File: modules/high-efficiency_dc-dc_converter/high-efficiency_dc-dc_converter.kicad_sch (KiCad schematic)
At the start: 11 parts

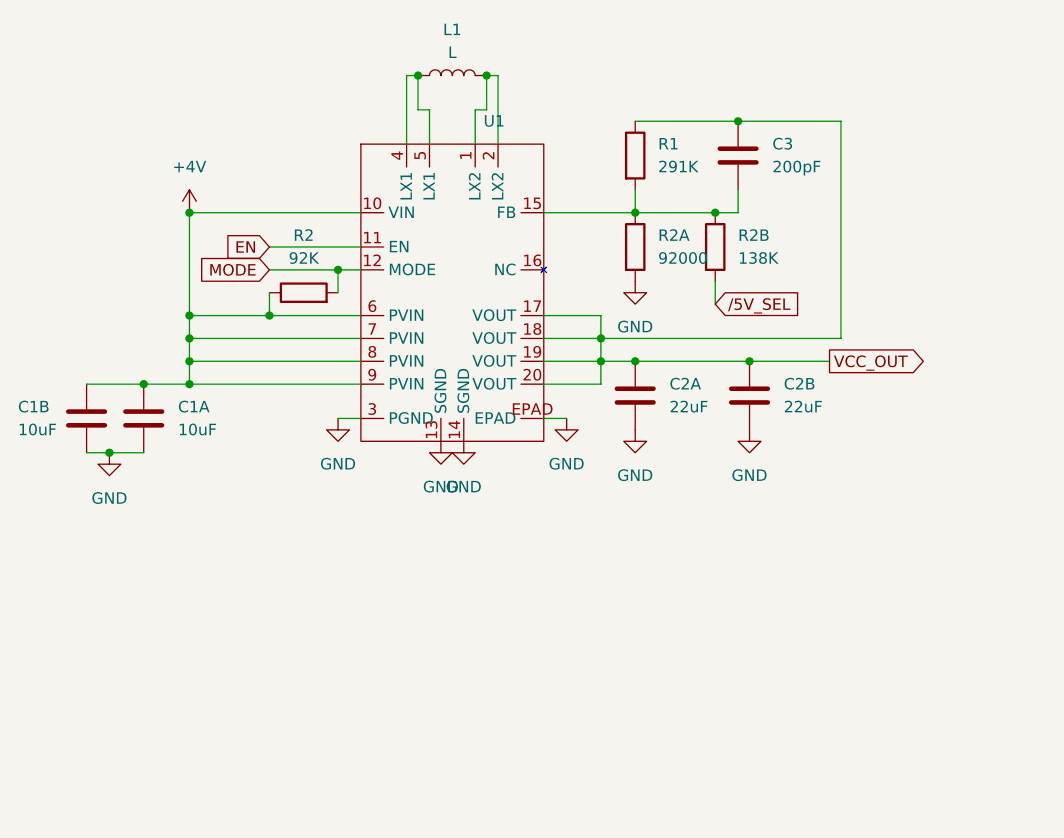
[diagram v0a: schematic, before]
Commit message: assign footprints for passives for DC:DC converter module
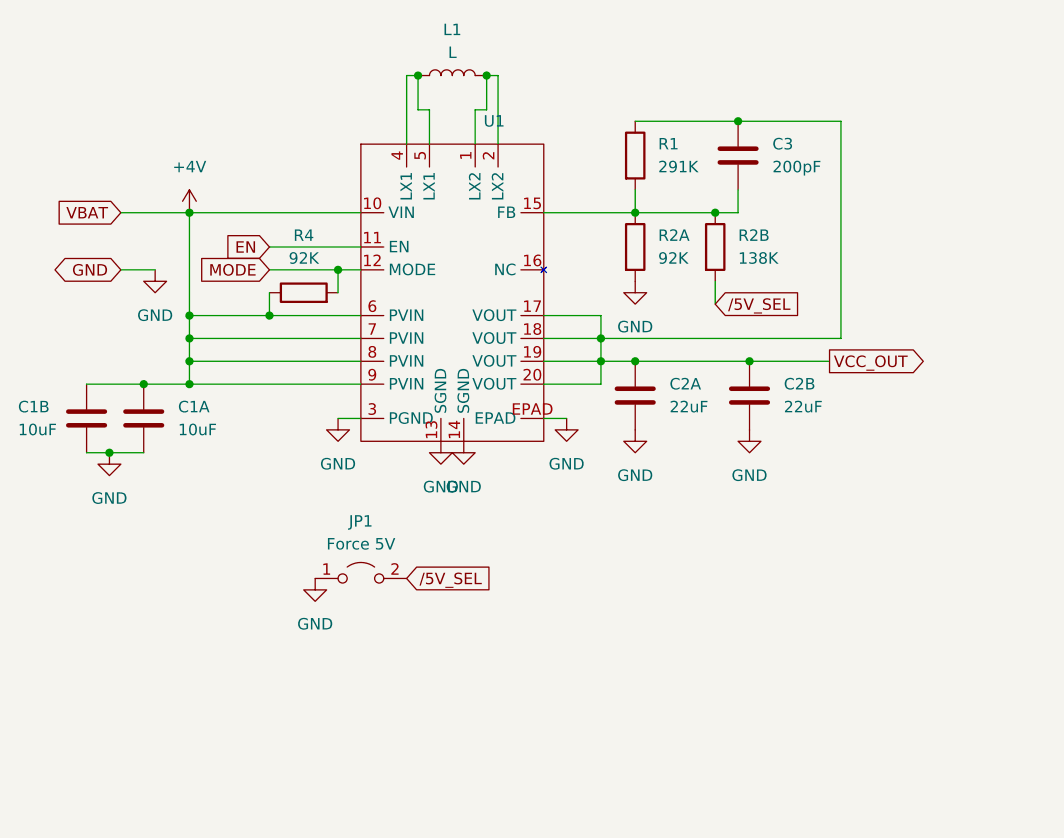
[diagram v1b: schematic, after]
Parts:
- added JP1: Force 5V, Jumper:SolderJumper-2_P1.3mm_Open_RoundedPad1.0x1.5mm, symbol Jumper:Jumper_2_Open
- C1A, C1B, C2A, C2B, C3: footprint (none) -> Capacitor_SMD:C_0805_2012Metric
- L1: footprint (none) -> Inductor_SMD:L_1008_2520Metric
- R1, R2B: footprint (none) -> Resistor_SMD:R_0603_1608Metric
- R2A: value 92000 -> 92K; footprint (none) -> Resistor_SMD:R_0603_1608Metric
- R4: renamed from R2; footprint (none) -> Resistor_SMD:R_0603_1608Metric
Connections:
- net GND: now also JP1.1 (A)
- net /5V_SEL: now also JP1.2 (B)
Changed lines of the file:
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@@
   (junction (at 38.1 77.47) (diameter 0) (color 0 0 0 0)
   )
+  (wire (pts (xy 35.56 58.42) (xy 43.18 58.42))
+    (stroke (width 0) (type default))
+  )
   (wire (pts (xy 82.55 77.47) (xy 88.9 77.47))
     (stroke (width 0) (type default))
@@
     (stroke (width 0) (type default))
   )
+  (wire (pts (xy 35.56 64.77) (xy 39.37 64.77))
+    (stroke (width 0) (type default))
+  )
   (wire (pts (xy 43.18 77.47) (xy 62.23 77.47))
     (stroke (width 0) (type default))
@@
   (wire (pts (xy 68.58 43.18) (xy 67.31 43.18))
     (stroke (width 0) (type default))
+  )
+  (global_label "{slash}5V_SEL" (shape input) (at 67.31 99.06 0) (fields_autoplaced)
+    (effects (font (size 1.27 1.27)) (justify left))
+    (property "Intersheetrefs" "${INTERSHEET_REFS}" (at 78.278 99.06 0)
+      (effects (font (size 1.27 1.27)) (justify left) hide)
+    )
   )
   (global_label "MODE" (shape input) (at 52.07 64.77 180) (fields_autoplaced)
@@
     )
   )
+  (global_label "VBAT" (shape input) (at 35.56 58.42 180) (fields_autoplaced)
+    (effects (font (size 1.27 1.27)) (justify right))
+    (property "Intersheetrefs" "${INTERSHEET_REFS}" (at 28.16 58.42 0)
+      (effects (font (size 1.27 1.27)) (justify right) hide)
+    )
+  )
   (global_label "{slash}5V_SEL" (shape input) (at 101.6 68.58 0) (fields_autoplaced)
     (effects (font (size 1.27 1.27)) (justify left))
@@
     )
   )
+  (global_label "GND" (shape bidirectional) (at 35.56 64.77 180) (fields_autoplaced)
+    (effects (font (size 1.27 1.27)) (justify right))
+    (property "Intersheetrefs" "${INTERSHEET_REFS}" (at 27.593 64.77 0)
+      (effects (font (size 1.27 1.27)) (justify right) hide)
+    )
+  )
   (global_label "VCC_OUT" (shape output) (at 114.3 74.93 0) (fields_autoplaced)
     (effects (font (size 1.27 1.27)) (justify left))
@@
       (effects (font (size 1.27 1.27)) (justify left))
     )
-    (property "Footprint" "" (at 99.822 62.23 90)
+    (property "Footprint" "Resistor_SMD:R_0603_1608Metric" (at 99.822 62.23 90)
       (effects (font (size 1.27 1.27)) hide)
     )
@@
       (effects (font (size 1.27 1.27)) (justify left))
     )
-    (property "Footprint" "" (at 90.932 52.07 90)
+    (property "Footprint" "Resistor_SMD:R_0603_1608Metric" (at 90.932 52.07 90)
       (effects (font (size 1.27 1.27)) hide)
     )
@@
         (path "/7f4a2112-cc8e-483f-9ea5-76225b466e70"
           (reference "#PWR03") (unit 1)
+        )
+      )
+    )
+  )
+  (symbol (lib_id "power:GND") (at 57.15 99.06 0) (unit 1)
+    (in_bom yes) (on_board yes) (dnp no) (fields_autoplaced)
+    (property "Reference" "#PWR011" (at 57.15 105.41 0)
+      (effects (font (size 1.27 1.27)) hide)
+    )
+    (property "Value" "GND" (at 57.15 104.14 0)
+      (effects (font (size 1.27 1.27)))
+    )
+    (property "Footprint" "" (at 57.15 99.06 0)
+      (effects (font (size 1.27 1.27)) hide)
+    )
+    (property "Datasheet" "" (at 57.15 99.06 0)
+      (effects (font (size 1.27 1.27)) hide)
+    )
+    (pin "1")
+    (instances
+      (project "high-efficiency_dc-dc_converter"
+        (path "/7f4a2112-cc8e-483f-9ea5-76225b466e70"
+          (reference "#PWR011") (unit 1)
         )
       )
@@
       (effects (font (size 1.27 1.27)) (justify left))
     )
-    (property "Value" "92000" (at 95.25 63.5 0)
-      (effects (font (size 1.27 1.27)) (justify left))
-    )
-    (property "Footprint" "" (at 90.932 62.23 90)
+    (property "Value" "92K" (at 95.25 63.5 0)
+      (effects (font (size 1.27 1.27)) (justify left))
+    )
+    (property "Footprint" "Resistor_SMD:R_0603_1608Metric" (at 90.932 62.23 90)
       (effects (font (size 1.27 1.27)) hide)
     )
@@
     )
   )
+  (symbol (lib_id "power:GND") (at 39.37 64.77 0) (unit 1)
+    (in_bom yes) (on_board yes) (dnp no) (fields_autoplaced)
+    (property "Reference" "#PWR010" (at 39.37 71.12 0)
+      (effects (font (size 1.27 1.27)) hide)
+    )
+    (property "Value" "GND" (at 39.37 69.85 0)
+      (effects (font (size 1.27 1.27)))
+    )
+    (property "Footprint" "" (at 39.37 64.77 0)
+      (effects (font (size 1.27 1.27)) hide)
+    )
+    (property "Datasheet" "" (at 39.37 64.77 0)
+      (effects (font (size 1.27 1.27)) hide)
+    )
+    (pin "1")
+    (instances
+      (project "high-efficiency_dc-dc_converter"
+        (path "/7f4a2112-cc8e-483f-9ea5-76225b466e70"
+          (reference "#PWR010") (unit 1)
+        )
+      )
+    )
+  )
   (symbol (lib_id "Device:R") (at 55.88 67.31 90) (unit 1)
     (in_bom yes) (on_board yes) (dnp no) (fields_autoplaced)
-    (property "Reference" "R2" (at 55.88 60.96 90)
+    (property "Reference" "R4" (at 55.88 60.96 90)
       (effects (font (size 1.27 1.27)))
     )
@@
       (effects (font (size 1.27 1.27)))
     )
-    (property "Footprint" "" (at 55.88 69.088 90)
+    (property "Footprint" "Resistor_SMD:R_0603_1608Metric" (at 55.88 69.088 90)
       (effects (font (size 1.27 1.27)) hide)
     )
@@
       (project "high-efficiency_dc-dc_converter"
         (path "/7f4a2112-cc8e-483f-9ea5-76225b466e70"
-          (reference "R2") (unit 1)
+          (reference "R4") (unit 1)
         )
       )
@@
       (effects (font (size 1.27 1.27)) (justify left))
     )
-    (property "Footprint" "" (at 32.7152 85.09 0)
+    (property "Footprint" "Capacitor_SMD:C_0805_2012Metric" (at 32.7152 85.09 0)
       (effects (font (size 1.27 1.27)) hide)
     )
@@
       (effects (font (size 1.27 1.27)) (justify left))
     )
-    (property "Footprint" "" (at 105.1052 55.88 0)
+    (property "Footprint" "Capacitor_SMD:C_0805_2012Metric" (at 105.1052 55.88 0)
       (effects (font (size 1.27 1.27)) hide)
     )
@@
     )
   )
+  (symbol (lib_id "Jumper:Jumper_2_Open") (at 62.23 99.06 0) (unit 1)
+    (in_bom yes) (on_board yes) (dnp no) (fields_autoplaced)
+    (property "Reference" "JP1" (at 62.23 92.71 0)
+      (effects (font (size 1.27 1.27)))
+    )
+    (property "Value" "Force 5V" (at 62.23 95.25 0)
+      (effects (font (size 1.27 1.27)))
+    )
+    (property "Footprint" "Jumper:SolderJumper-2_P1.3mm_Open_RoundedPad1.0x1.5mm" (at 62.23 99.06 0)
+      (effects (font (size 1.27 1.27)) hide)
+    )
+    (property "Datasheet" "~" (at 62.23 99.06 0)
+      (effects (font (size 1.27 1.27)) hide)
+    )
+    (pin "1")
+    (pin "2")
+    (instances
+      (project "high-efficiency_dc-dc_converter"
+        (path "/7f4a2112-cc8e-483f-9ea5-76225b466e70"
+          (reference "JP1") (unit 1)
+        )
+      )
+    )
+  )
   (symbol (lib_id "Device:C") (at 38.1 81.28 0) (unit 1)
     (in_bom yes) (on_board yes) (dnp no) (fields_autoplaced)
@@
       (effects (font (size 1.27 1.27)) (justify left))
     )
-    (property "Footprint" "" (at 39.0652 85.09 0)
+    (property "Footprint" "Capacitor_SMD:C_0805_2012Metric" (at 39.0652 85.09 0)
       (effects (font (size 1.27 1.27)) hide)
     )
@@
       (effects (font (size 1.27 1.27)) (justify left))
     )
-    (property "Footprint" "" (at 93.6752 82.55 0)
+    (property "Footprint" "Capacitor_SMD:C_0805_2012Metric" (at 93.6752 82.55 0)
       (effects (font (size 1.27 1.27)) hide)
     )
@@
       (effects (font (size 1.27 1.27)) (justify left))
     )
-    (property "Footprint" "" (at 106.3752 82.55 0)
+    (property "Footprint" "Capacitor_SMD:C_0805_2012Metric" (at 106.3752 82.55 0)
       (effects (font (size 1.27 1.27)) hide)
     )
@@
       (effects (font (size 1.27 1.27)))
     )
-    (property "Footprint" "" (at 72.39 43.18 0)
-      (effects (font (size 1.27 1.27)) hide)
-    )
+    (property "Footprint" "Inductor_SMD:L_1008_2520Metric" (at 72.39 43.18 0)
+      (effects (font (size 1.27 1.27)) hide)
+    )

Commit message: add QFN20 footprint for DC:DC converter IC
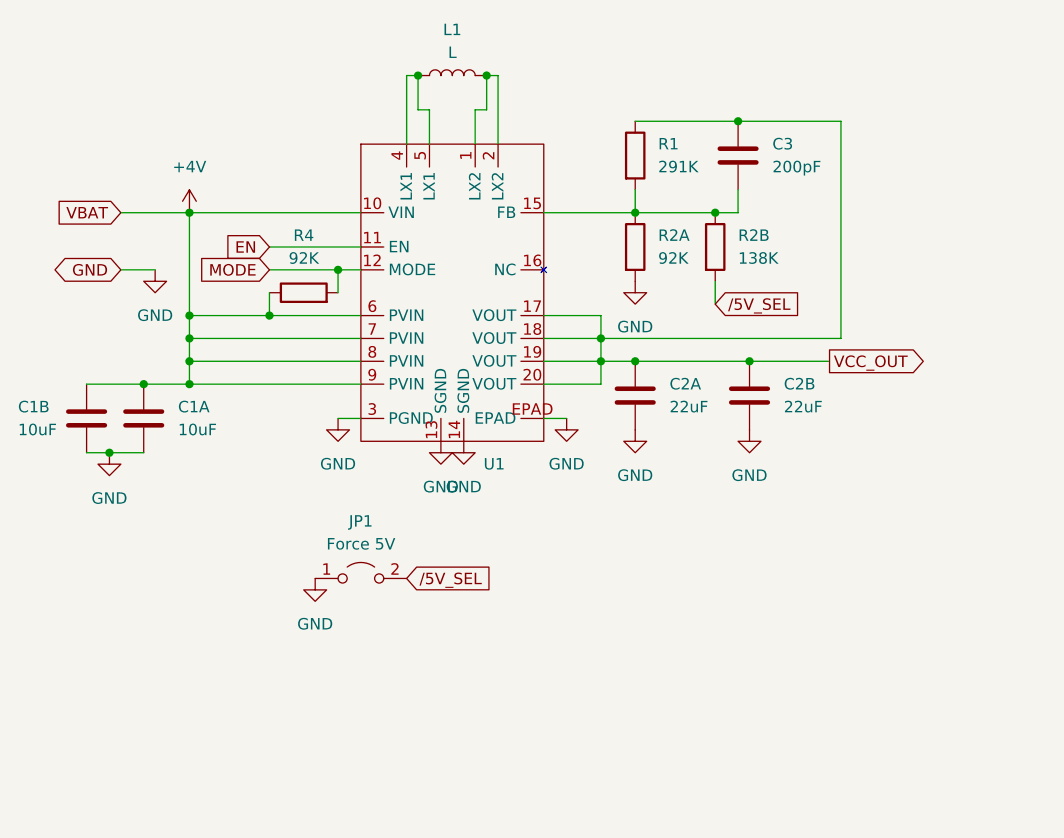
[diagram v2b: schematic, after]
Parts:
- U1: footprint (none) -> QFN20:QFN50P400X400X90-21N
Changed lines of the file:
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@@
   (symbol (lib_id "ISL91127:ISL91127IRAZ") (at 72.39 67.31 0) (unit 1)
     (in_bom yes) (on_board yes) (dnp no) (fields_autoplaced)
-    (property "Reference" "U1" (at 75.8541 48.26 0)
+    (property "Reference" "U1" (at 75.8541 86.36 0)
       (effects (font (size 1.27 1.27)) (justify left))
     )
@@
       (effects (font (size 1.27 1.27)))
     )
-    (property "Footprint" "" (at 60.96 66.04 0)
+    (property "Footprint" "QFN20:QFN50P400X400X90-21N" (at 60.96 66.04 0)
       (effects (font (size 1.27 1.27)) hide)
     )

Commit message: update schematic, slightly compact PCB layout
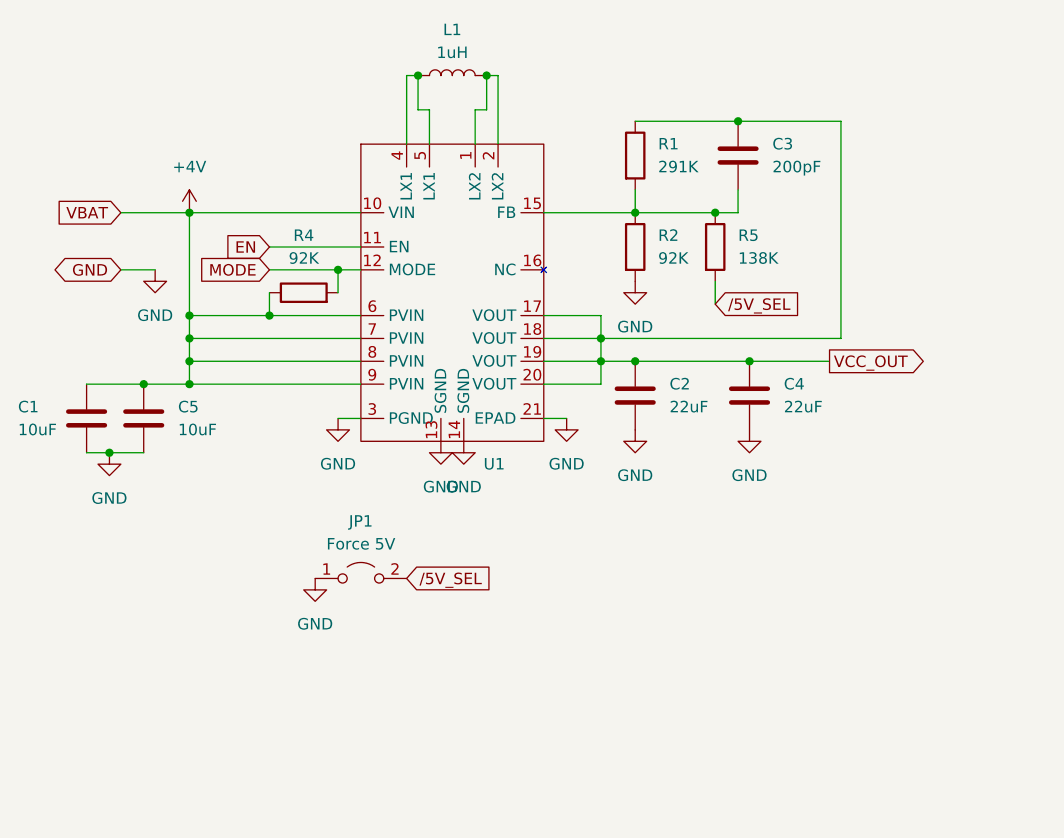
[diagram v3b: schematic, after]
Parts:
- L1: value L -> 1uH
- renumbered C1B to C1, C2A to C2, C2B to C4, C1A to C5, R2A to R2, R2B to R5
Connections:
- net GND: now also U1.21 (EPAD); no longer U1.EPAD
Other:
- moved on the sheet: U1
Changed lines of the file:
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@@
   (symbol (lib_id "Device:R") (at 101.6 62.23 0) (unit 1)
     (in_bom yes) (on_board yes) (dnp no) (fields_autoplaced)
-    (property "Reference" "R2B" (at 104.14 60.96 0)
+    (property "Reference" "R5" (at 104.14 60.96 0)
       (effects (font (size 1.27 1.27)) (justify left))
     )
@@
       (project "high-efficiency_dc-dc_converter"
         (path "/7f4a2112-cc8e-483f-9ea5-76225b466e70"
-          (reference "R2B") (unit 1)
+          (reference "R5") (unit 1)
         )
       )
@@
     )
     (pin "5")
-    (pin "EPAD")
+    (pin "21")
     (pin "1")
     (pin "9")
@@
   (symbol (lib_id "Device:R") (at 92.71 62.23 0) (unit 1)
     (in_bom yes) (on_board yes) (dnp no) (fields_autoplaced)
-    (property "Reference" "R2A" (at 95.25 60.96 0)
+    (property "Reference" "R2" (at 95.25 60.96 0)
       (effects (font (size 1.27 1.27)) (justify left))
     )
@@
       (project "high-efficiency_dc-dc_converter"
         (path "/7f4a2112-cc8e-483f-9ea5-76225b466e70"
-          (reference "R2A") (unit 1)
+          (reference "R2") (unit 1)
         )
       )
@@
   (symbol (lib_id "Device:C") (at 31.75 81.28 0) (unit 1)
     (in_bom yes) (on_board yes) (dnp no)
-    (property "Reference" "C1B" (at 24.13 80.01 0)
+    (property "Reference" "C1" (at 24.13 80.01 0)
       (effects (font (size 1.27 1.27)) (justify left))
     )
@@
       (project "high-efficiency_dc-dc_converter"
         (path "/7f4a2112-cc8e-483f-9ea5-76225b466e70"
-          (reference "C1B") (unit 1)
+          (reference "C1") (unit 1)
         )
       )
@@
   (symbol (lib_id "Device:C") (at 38.1 81.28 0) (unit 1)
     (in_bom yes) (on_board yes) (dnp no) (fields_autoplaced)
-    (property "Reference" "C1A" (at 41.91 80.01 0)
+    (property "Reference" "C5" (at 41.91 80.01 0)
       (effects (font (size 1.27 1.27)) (justify left))
     )
@@
       (project "high-efficiency_dc-dc_converter"
         (path "/7f4a2112-cc8e-483f-9ea5-76225b466e70"
-          (reference "C1A") (unit 1)
+          (reference "C5") (unit 1)
         )
       )
@@
   (symbol (lib_id "Device:C") (at 92.71 78.74 0) (unit 1)
     (in_bom yes) (on_board yes) (dnp no) (fields_autoplaced)
-    (property "Reference" "C2A" (at 96.52 77.47 0)
+    (property "Reference" "C2" (at 96.52 77.47 0)
       (effects (font (size 1.27 1.27)) (justify left))
     )
@@
       (project "high-efficiency_dc-dc_converter"
         (path "/7f4a2112-cc8e-483f-9ea5-76225b466e70"
-          (reference "C2A") (unit 1)
+          (reference "C2") (unit 1)
         )
       )
@@
   (symbol (lib_id "Device:C") (at 105.41 78.74 0) (unit 1)
     (in_bom yes) (on_board yes) (dnp no) (fields_autoplaced)
-    (property "Reference" "C2B" (at 109.22 77.47 0)
+    (property "Reference" "C4" (at 109.22 77.47 0)
       (effects (font (size 1.27 1.27)) (justify left))
     )
@@
       (project "high-efficiency_dc-dc_converter"
         (path "/7f4a2112-cc8e-483f-9ea5-76225b466e70"
-          (reference "C2B") (unit 1)
+          (reference "C4") (unit 1)
         )
       )
@@
       (effects (font (size 1.27 1.27)))
     )
-    (property "Value" "L" (at 72.39 40.64 90)
-      (effects (font (size 1.27 1.27)))
-    )
+    (property "Value" "1uH" (at 72.39 40.64 90)
+      (effects (font (size 1.27 1.27)))
+    )
